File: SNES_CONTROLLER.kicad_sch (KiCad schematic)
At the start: 24 parts, among them J1 Screw_Terminal_01x07, J2 Screw_Terminal_01x12, J3 Screw_Terminal_01x12, U1 4021, U2 4021

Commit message: development
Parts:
- added R20: R, Resistor_THT:R_Axial_DIN0204_L3.6mm_D1.6mm_P7.62mm_Horizontal, symbol Device:R
- U2: footprint (none) -> Package_DIP:DIP-16_W7.62mm
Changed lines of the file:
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@@
+	(symbol
+		(lib_id "Device:R")
+		(at 208.28 142.24 0)
+		(unit 1)
+		(exclude_from_sim no)
+		(in_bom yes)
+		(on_board yes)
+		(dnp no)
+		(fields_autoplaced yes)
+		(property "Reference" "R20"
+			(at 210.82 140.9699 0)
+			(effects
+				(font
+					(size 1.27 1.27)
+				)
+				(justify left)
+			)
+		)
+		(property "Value" "R"
+			(at 210.82 143.5099 0)
+			(effects
+				(font
+					(size 1.27 1.27)
+				)
+				(justify left)
+			)
+		)
+		(property "Footprint" "Resistor_THT:R_Axial_DIN0204_L3.6mm_D1.6mm_P7.62mm_Horizontal"
+			(at 206.502 142.24 90)
+			(effects
+				(font
+					(size 1.27 1.27)
+				)
+				(hide yes)
+			)
+		)
+		(property "Datasheet" "~"
+			(at 208.28 142.24 0)
+			(effects
+				(font
+					(size 1.27 1.27)
+				)
+				(hide yes)
+			)
+		)
+		(property "Description" "Resistor"
+			(at 208.28 142.24 0)
+			(effects
+				(font
+					(size 1.27 1.27)
+				)
+				(hide yes)
+			)
+		)
+		(pin "1"
+		)
+		(pin "2"
+		)
+		(instances
+			(project ""
+				(path "/719592b0-85a8-4eb6-8d13-f447981f3475"
+					(reference "R20")
+					(unit 1)
+				)
+			)
+		)
+	)
 	(symbol
 		(lib_id "Device:R")
@@
 			)
 		)
-		(property "Footprint" ""
+		(property "Footprint" "Package_DIP:DIP-16_W7.62mm"
 			(at 143.51 138.43 0)
 			(effects

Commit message: SNES HW controller Version 1.0
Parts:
- removed R20: R, Resistor_THT:R_Axial_DIN0204_L3.6mm_D1.6mm_P7.62mm_Horizontal, symbol Device:R
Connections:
- net Clk: now also U1.10 (CP), U2.10 (CP)
- net Data1: now also U1.3 (Q7)
- net Latch: now also U1.9 (PL), U2.9 (PL)
- net at U1.11 (DS): now also U2.3 (Q7)
- no-connect marks 2 -> 7
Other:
- moved on the sheet: U1, U2

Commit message: SNES CONTROLLER v2
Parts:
- removed J1: Screw_Terminal_01x07, TerminalBlock:TerminalBlock_MaiXu_MX126-5.0-07P_1x07_P5.00mm, symbol Connector:Screw_Terminal_01x07
- added J4: Screw_Terminal_01x05, TerminalBlock:TerminalBlock_MaiXu_MX126-5.0-05P_1x05_P5.00mm, symbol Connector:Screw_Terminal_01x05
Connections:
- net Clk: now also J4.2 (Pin_2)
- net Data1: now also J4.4 (Pin_4)
- net Gnd: now also J4.5 (Pin_5)
- net Latch: now also J4.3 (Pin_3)
- net Vcc: now also J4.1 (Pin_1)
- no-connect marks 7 -> 5
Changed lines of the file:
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@@
+	)
+	(junction
+		(at 142.24 95.25)
+		(diameter 0)
+		(color 0 0 0 0)
 	)
 	(junction
@@
 	)
 	(junction
-		(at 140.97 95.25)
+		(at 181.61 110.49)
 		(diameter 0)
 		(color 0 0 0 0)
@@
 	(junction
 		(at 107.95 40.64)
-		(diameter 0)
-		(color 0 0 0 0)
-	)
-	(junction
-		(at 181.61 115.57)
 		(diameter 0)
 		(color 0 0 0 0)
@@
 	)
 	(no_connect
-		(at 205.74 110.49)
-	)
-	(no_connect
 		(at 161.29 129.54)
 	)
@@
 	)
 	(no_connect
-		(at 205.74 113.03)
-	)
-	(no_connect
 		(at 140.97 134.62)
 	)
@@
 	(wire
 		(pts
-			(xy 205.74 105.41) (xy 182.88 105.41)
+			(xy 182.88 105.41) (xy 210.82 105.41)
 		)
 		(stroke
@@
 	(wire
 		(pts
-			(xy 181.61 115.57) (xy 205.74 115.57)
-		)
-		(stroke
-			(width 0)
-			(type default)
-		)
-	)
-	(wire
-		(pts
 			(xy 45.72 80.01) (xy 45.72 74.93)
 		)
@@
 	(wire
 		(pts
-			(xy 140.97 95.25) (xy 140.97 115.57)
+			(xy 142.24 95.25) (xy 142.24 110.49)
 		)
 		(stroke
@@
 	(wire
 		(pts
-			(xy 205.74 102.87) (xy 191.77 102.87)
+			(xy 191.77 102.87) (xy 210.82 102.87)
 		)
 		(stroke
@@
 	(wire
 		(pts
-			(xy 199.39 100.33) (xy 205.74 100.33)
+			(xy 199.39 100.33) (xy 210.82 100.33)
 		)
 		(stroke
@@
 	(wire
 		(pts
-			(xy 181.61 115.57) (xy 181.61 162.56)
-		)
-		(stroke
-			(width 0)
-			(type default)
-		)
-	)
-	(wire
-		(pts
 			(xy 38.1 67.31) (xy 95.25 67.31)
 		)
@@
 	(wire
 		(pts
-			(xy 140.97 115.57) (xy 181.61 115.57)
+			(xy 142.24 110.49) (xy 181.61 110.49)
 		)
 		(stroke
@@
 	(wire
 		(pts
-			(xy 205.74 107.95) (xy 175.26 107.95)
+			(xy 175.26 107.95) (xy 210.82 107.95)
 		)
 		(stroke
@@
 	(wire
 		(pts
+			(xy 181.61 110.49) (xy 210.82 110.49)
+		)
+		(stroke
+			(width 0)
+			(type default)
+		)
+	)
+	(wire
+		(pts
 			(xy 82.55 149.86) (xy 82.55 154.94)
 		)
@@
 	(wire
 		(pts
-			(xy 45.72 95.25) (xy 140.97 95.25)
+			(xy 45.72 95.25) (xy 142.24 95.25)
 		)
 		(stroke
@@
 	(wire
 		(pts
+			(xy 181.61 110.49) (xy 181.61 162.56)
+		)
+		(stroke
+			(width 0)
+			(type default)
+		)
+	)
+	(wire
+		(pts
 			(xy 107.95 144.78) (xy 107.95 115.57)
 		)
@@
 	(wire
 		(pts
-			(xy 149.86 95.25) (xy 140.97 95.25)
+			(xy 149.86 95.25) (xy 142.24 95.25)
 		)
 		(stroke
@@
 	)
 	(label "Gnd"
-		(at 201.93 115.57 0)
+		(at 207.01 110.49 0)
 		(effects
 			(font
@@
 				(path "/719592b0-85a8-4eb6-8d13-f447981f3475"
 					(reference "R7")
-					(unit 1)
-				)
-			)
-		)
-	)
-	(symbol
-		(lib_id "Connector:Screw_Terminal_01x07")
-		(at 210.82 107.95 0)
-		(unit 1)
-		(exclude_from_sim no)
-		(in_bom yes)
-		(on_board yes)
-		(dnp no)
-		(fields_autoplaced yes)
-		(property "Reference" "J1"
-			(at 213.36 106.6799 0)
-			(effects
-				(font
-					(size 1.27 1.27)
-				)
-				(justify left)
-			)
-		)
-		(property "Value" "Screw_Terminal_01x07"
-			(at 213.36 109.2199 0)
-			(effects
-				(font
-					(size 1.27 1.27)
-				)
-				(justify left)
-			)
-		)
-		(property "Footprint" "TerminalBlock:TerminalBlock_MaiXu_MX126-5.0-07P_1x07_P5.00mm"
-			(at 210.82 107.95 0)
-			(effects
-				(font
-					(size 1.27 1.27)
-				)
-				(hide yes)
-			)
-		)
-		(property "Datasheet" "~"
-			(at 210.82 107.95 0)
-			(effects
-				(font
-					(size 1.27 1.27)
-				)
-				(hide yes)
-			)
-		)
-		(property "Description" "Generic screw terminal, single row, 01x07, script generated (kicad-library-utils/schlib/autogen/connector/)"
-			(at 210.82 107.95 0)
-			(effects
-				(font
-					(size 1.27 1.27)
-				)
-				(hide yes)
-			)
-		)
-		(pin "7"
-		)
-		(pin "6"
-		)
-		(pin "5"
-		)
-		(pin "4"
-		)
-		(pin "2"
-		)
-		(pin "3"
-		)
-		(pin "1"
-		)
-		(instances
-			(project ""
-				(path "/719592b0-85a8-4eb6-8d13-f447981f3475"
-					(reference "J1")
 					(unit 1)
 				)
@@
 					(unit 1)
 				)
+			)
+		)
+	)
+	(symbol
+		(lib_id "Connector:Screw_Terminal_01x05")
+		(at 215.9 105.41 0)
+		(unit 1)
+		(exclude_from_sim no)
+		(in_bom yes)
+		(on_board yes)
+		(dnp no)
+		(fields_autoplaced yes)
+		(property "Reference" "J4"
+			(at 218.44 104.1399 0)
+			(effects
+				(font
+					(size 1.27 1.27)
+				)
+				(justify left)
+			)
+		)
+		(property "Value" "Screw_Terminal_01x05"
+			(at 218.44 106.6799 0)
+			(effects
+				(font
+					(size 1.27 1.27)
+				)
+				(justify left)
+			)
+		)
+		(property "Footprint" "TerminalBlock:TerminalBlock_MaiXu_MX126-5.0-05P_1x05_P5.00mm"
+			(at 215.9 105.41 0)
+			(effects
+				(font
+					(size 1.27 1.27)
+				)
+				(hide yes)
+			)
+		)
+		(property "Datasheet" "~"
+			(at 215.9 105.41 0)
+			(effects
+				(font
+					(size 1.27 1.27)
+				)
+				(hide yes)
+			)
+		)
+		(property "Description" "Generic screw terminal, single row, 01x05, script generated (kicad-library-utils/schlib/autogen/connector/)"
+			(at 215.9 105.41 0)
+			(effects
+				(font
+					(size 1.27 1.27)
+				)
+				(hide yes)
+			)
+		)
+		(pin "5"
+		)
+		(pin "1"
+		)
+		(pin "4"
+		)
+		(pin "3"
+		)
+		(pin "2"
+		)
+		(instances
+			(project ""
+				(path "/719592b0-85a8-4eb6-8d13-f447981f3475"
+					(reference "J4")
+					(unit 1)
+				)

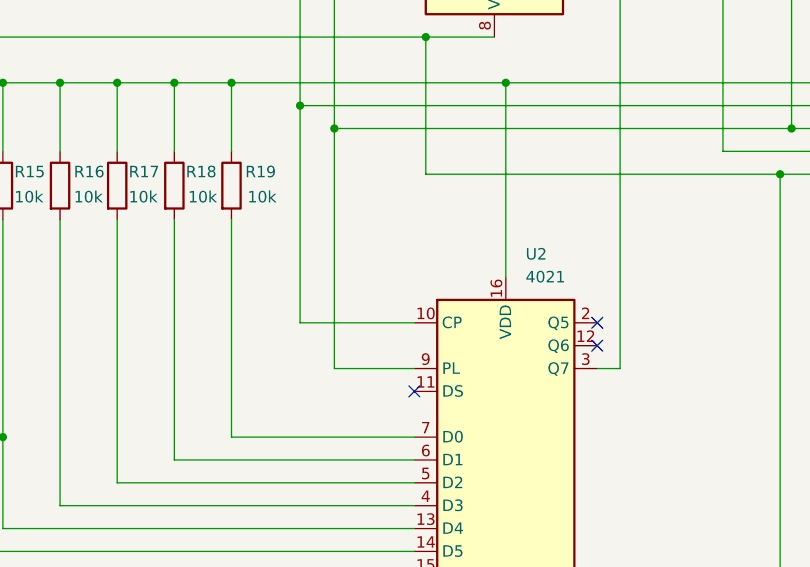
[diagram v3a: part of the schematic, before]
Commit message: Error corrected. Pin 11 of second 4021 connected to GND
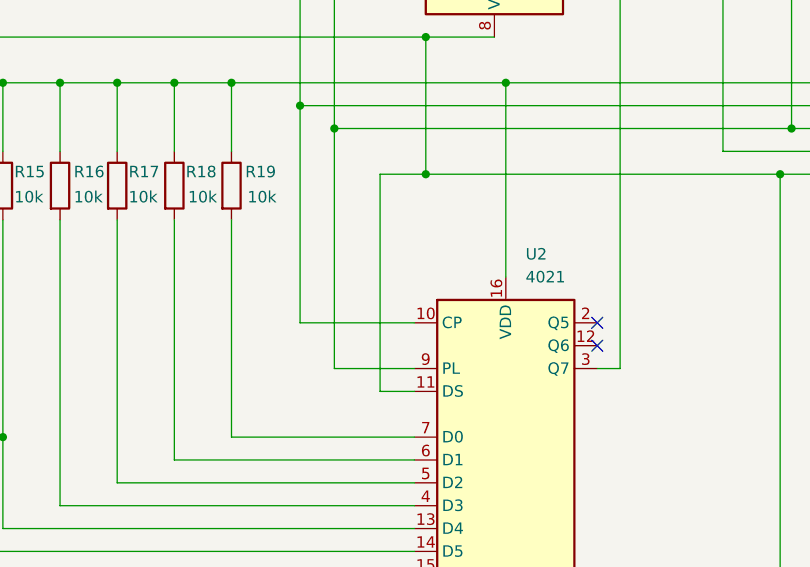
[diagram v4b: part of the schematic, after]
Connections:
- net Gnd: now also U2.11 (DS)
- no-connect marks 5 -> 4
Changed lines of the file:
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@@
+	)
+	(junction
+		(at 142.24 110.49)
+		(diameter 0)
+		(color 0 0 0 0)
 	)
 	(junction
@@
 		(at 160.02 62.23)
 	)
-	(no_connect
-		(at 140.97 134.62)
-	)
 	(wire
 		(pts
@@
 	(wire
 		(pts
+			(xy 137.16 134.62) (xy 137.16 110.49)
+		)
+		(stroke
+			(width 0)
+			(type default)
+		)
+	)
+	(wire
+		(pts
 			(xy 95.25 139.7) (xy 95.25 115.57)
 		)
@@
 	(wire
 		(pts
+			(xy 140.97 134.62) (xy 137.16 134.62)
+		)
+		(stroke
+			(width 0)
+			(type default)
+		)
+	)
+	(wire
+		(pts
 			(xy 181.61 110.49) (xy 210.82 110.49)
 		)
@@
 		)
 		(stroke
+			(width 0)
+			(type default)
+		)
+	)
+	(wire
+		(pts
+			(xy 137.16 110.49) (xy 142.24 110.49)
+		)
+		(stroke

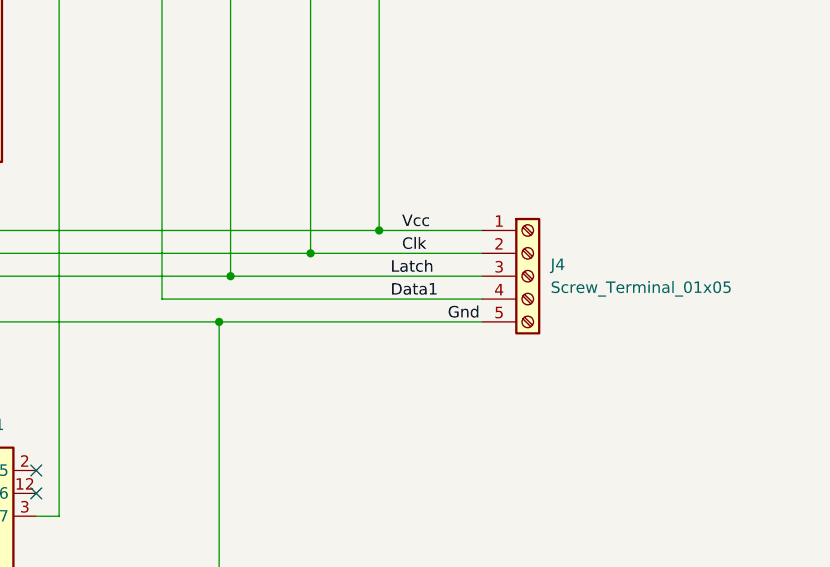
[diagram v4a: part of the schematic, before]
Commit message: changes reverted. Connector changed by a 6 pin one. Rounded PCB
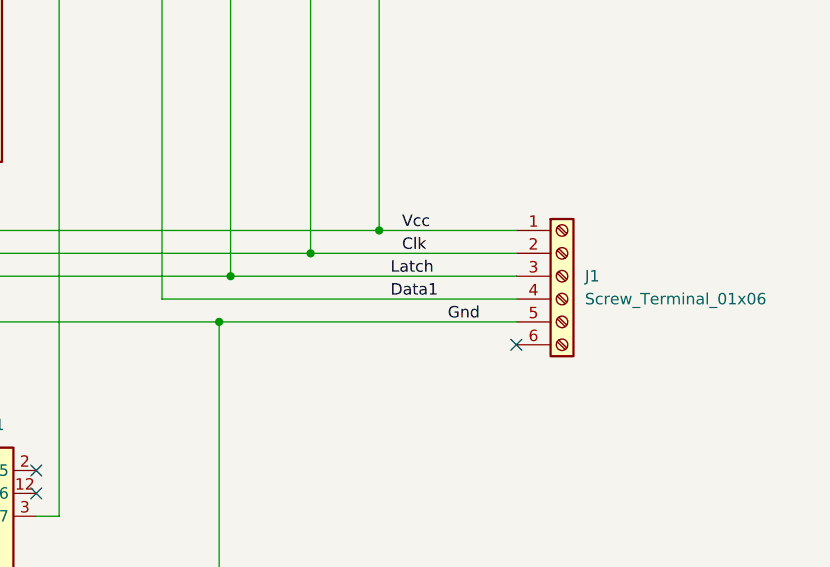
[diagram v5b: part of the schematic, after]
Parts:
- removed J4: Screw_Terminal_01x05, TerminalBlock:TerminalBlock_MaiXu_MX126-5.0-05P_1x05_P5.00mm, symbol Connector:Screw_Terminal_01x05
- added J1: Screw_Terminal_01x06, TerminalBlock:TerminalBlock_MaiXu_MX126-5.0-06P_1x06_P5.00mm, symbol Connector:Screw_Terminal_01x06
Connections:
- net Clk: now also J1.2 (Pin_2)
- net Data1: now also J1.4 (Pin_4)
- net Gnd: now also J1.5 (Pin_5)
- net Latch: now also J1.3 (Pin_3)
- net Vcc: now also J1.1 (Pin_1)
- no-connect marks 4 -> 5
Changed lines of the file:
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@@
+	)
+	(no_connect
+		(at 214.63 113.03)
 	)
 	(no_connect
@@
 	(wire
 		(pts
-			(xy 182.88 105.41) (xy 210.82 105.41)
+			(xy 182.88 105.41) (xy 214.63 105.41)
 		)
 		(stroke
@@
 	(wire
 		(pts
-			(xy 191.77 102.87) (xy 210.82 102.87)
+			(xy 191.77 102.87) (xy 214.63 102.87)
 		)
 		(stroke
@@
 	(wire
 		(pts
-			(xy 199.39 100.33) (xy 210.82 100.33)
+			(xy 199.39 100.33) (xy 214.63 100.33)
 		)
 		(stroke
@@
 	(wire
 		(pts
-			(xy 175.26 107.95) (xy 210.82 107.95)
+			(xy 175.26 107.95) (xy 214.63 107.95)
 		)
 		(stroke
@@
 	(wire
 		(pts
-			(xy 181.61 110.49) (xy 210.82 110.49)
+			(xy 181.61 110.49) (xy 214.63 110.49)
 		)
 		(stroke
@@
 				(path "/719592b0-85a8-4eb6-8d13-f447981f3475"
 					(reference "R4")
+					(unit 1)
+				)
+			)
+		)
+	)
+	(symbol
+		(lib_id "Connector:Screw_Terminal_01x06")
+		(at 219.71 105.41 0)
+		(unit 1)
+		(exclude_from_sim no)
+		(in_bom yes)
+		(on_board yes)
+		(dnp no)
+		(fields_autoplaced yes)
+		(property "Reference" "J1"
+			(at 222.25 105.4099 0)
+			(effects
+				(font
+					(size 1.27 1.27)
+				)
+				(justify left)
+			)
+		)
+		(property "Value" "Screw_Terminal_01x06"
+			(at 222.25 107.9499 0)
+			(effects
+				(font
+					(size 1.27 1.27)
+				)
+				(justify left)
+			)
+		)
+		(property "Footprint" "TerminalBlock:TerminalBlock_MaiXu_MX126-5.0-06P_1x06_P5.00mm"
+			(at 219.71 105.41 0)
+			(effects
+				(font
+					(size 1.27 1.27)
+				)
+				(hide yes)
+			)
+		)
+		(property "Datasheet" "~"
+			(at 219.71 105.41 0)
+			(effects
+				(font
+					(size 1.27 1.27)
+				)
+				(hide yes)
+			)
+		)
+		(property "Description" "Generic screw terminal, single row, 01x06, script generated (kicad-library-utils/schlib/autogen/connector/)"
+			(at 219.71 105.41 0)
+			(effects
+				(font
+					(size 1.27 1.27)
+				)
+				(hide yes)
+			)
+		)
+		(pin "3"
+		)
+		(pin "2"
+		)
+		(pin "1"
+		)
+		(pin "5"
+		)
+		(pin "4"
+		)
+		(pin "6"
+		)
+		(instances
+			(project ""
+				(path "/719592b0-85a8-4eb6-8d13-f447981f3475"
+					(reference "J1")
 					(unit 1)
 				)
@@
 					(unit 1)
 				)
-			)
-		)
-	)
-	(symbol
-		(lib_id "Connector:Screw_Terminal_01x05")
-		(at 215.9 105.41 0)
-		(unit 1)
-		(exclude_from_sim no)
-		(in_bom yes)
-		(on_board yes)
-		(dnp no)
-		(fields_autoplaced yes)
-		(property "Reference" "J4"
-			(at 218.44 104.1399 0)
-			(effects
-				(font
-					(size 1.27 1.27)
-				)
-				(justify left)
-			)
-		)
-		(property "Value" "Screw_Terminal_01x05"
-			(at 218.44 106.6799 0)
-			(effects
-				(font
-					(size 1.27 1.27)
-				)
-				(justify left)
-			)
-		)
-		(property "Footprint" "TerminalBlock:TerminalBlock_MaiXu_MX126-5.0-05P_1x05_P5.00mm"
-			(at 215.9 105.41 0)
-			(effects
-				(font
-					(size 1.27 1.27)
-				)
-				(hide yes)
-			)
-		)
-		(property "Datasheet" "~"
-			(at 215.9 105.41 0)
-			(effects
-				(font
-					(size 1.27 1.27)
-				)
-				(hide yes)
-			)
-		)
-		(property "Description" "Generic screw terminal, single row, 01x05, script generated (kicad-library-utils/schlib/autogen/connector/)"
-			(at 215.9 105.41 0)
-			(effects
-				(font
-					(size 1.27 1.27)
-				)
-				(hide yes)
-			)
-		)
-		(pin "5"
-		)
-		(pin "1"
-		)
-		(pin "4"
-		)
-		(pin "3"
-		)
-		(pin "2"
-		)
-		(instances
-			(project ""
-				(path "/719592b0-85a8-4eb6-8d13-f447981f3475"
-					(reference "J4")
-					(unit 1)
-				)
